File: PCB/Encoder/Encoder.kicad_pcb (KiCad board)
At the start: 2 copper layers, 44.3 x 44.8 mm, 8 parts, among them J1 1-1734595-0 Header, U1 AS5047P-ATSM

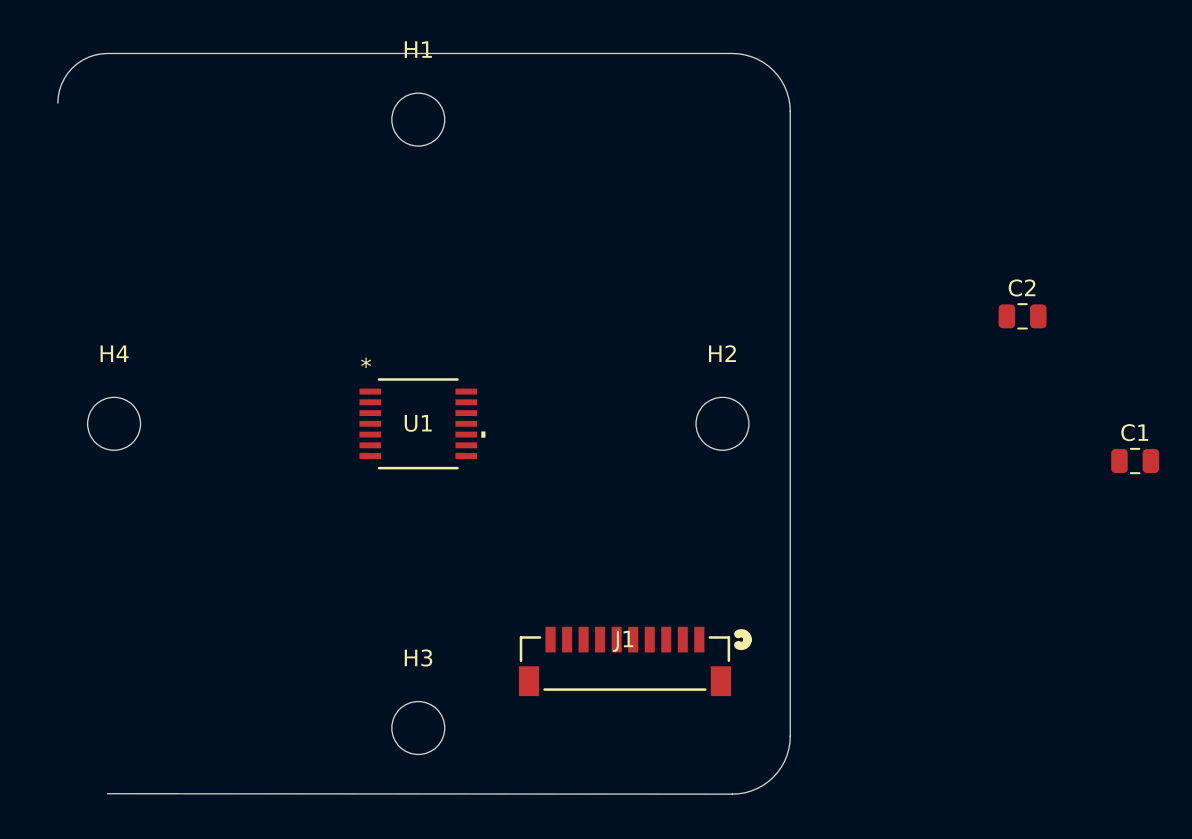
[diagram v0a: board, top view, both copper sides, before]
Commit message: Fixed GroundDetch not grounded
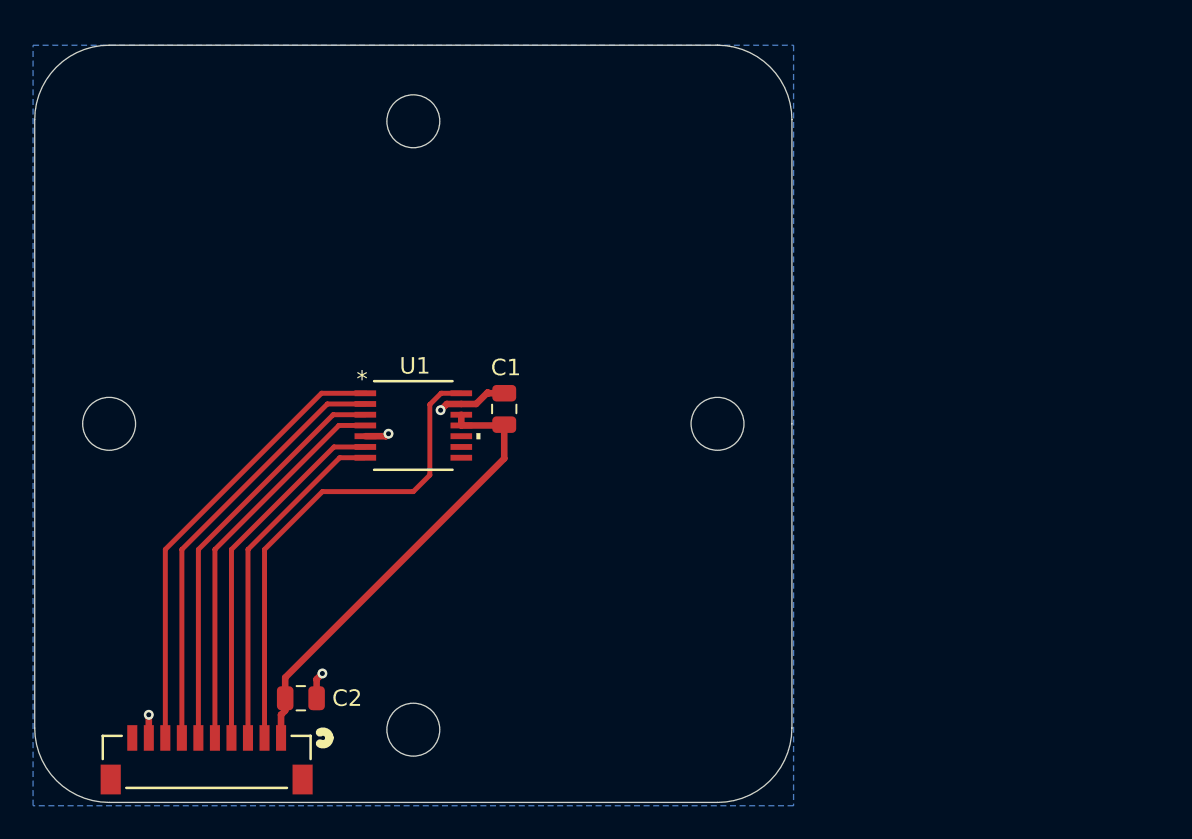
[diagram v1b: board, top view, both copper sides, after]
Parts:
- moved C2 49.4 mm to (125.2, 99.0)
- moved C1 38.3 mm to (137.5, 81.5), turned to 90 degrees
- moved J1 26.0 mm to (119.5, 102.8)
- moved H3 0.32 mm to (132.0, 100.9)
- moved H1 0.32 mm to (132.0, 64.1)
- moved U1 0.32 mm to (132.0, 82.5)
- moved H4 0.30 mm to (113.6, 82.4)
- moved H2 0.30 mm to (150.4, 82.4)
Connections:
- J1 pad 2: CS_ -> I
- J1 pad 3: CLK -> B
- J1 pad 4: MISO -> A
- J1 pad 6: A -> MISO
- J1 pad 7: B -> CLK
- J1 pad 8: I -> CS_
- U1 pad 5: Net-(U1-TEST) -> GND
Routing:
- net I: track 0.00 -> 29.7 mm
- net +3.3V: track 0.00 -> 27.9 mm
- net CS_: track 0.00 -> 27.4 mm
- net CLK: track 0.00 -> 26.1 mm
- net MISO: track 0.00 -> 24.9 mm
- net MOSI: track 0.00 -> 23.6 mm
- net A: track 0.00 -> 22.1 mm
- net B: track 0.00 -> 20.8 mm
- net GND: track 0.00 -> 8.83 mm, vias 0 -> 4
- added copper zone on B.Cu, net GND
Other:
- board size 44.3 x 44.8 mm -> 45.8 x 45.8 mm

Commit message: Connectors wrong side fixed, PCB v1.0 Done
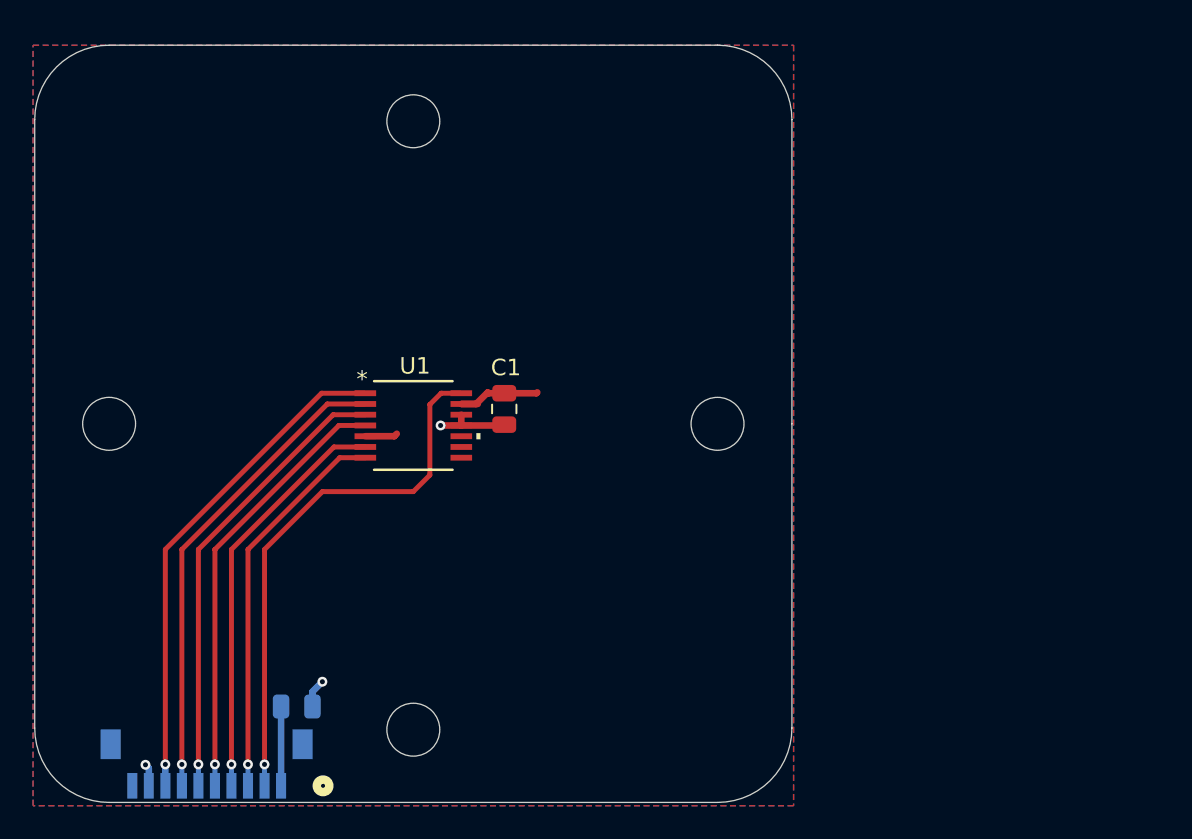
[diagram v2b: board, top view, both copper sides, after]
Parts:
- C2, J1: moved to B.Cu
- moved C2 0.56 mm to (125.0, 99.5)
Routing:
- net +3.3V: track 27.9 -> 9.39 mm, vias 0 -> 1
- net MOSI: track 23.6 -> 26.5 mm, vias 0 -> 1
- net MISO: track 24.9 -> 27.8 mm, vias 0 -> 1
- net I: track 29.7 -> 32.6 mm, vias 0 -> 1
- net CS_: track 27.4 -> 30.3 mm, vias 0 -> 1
- net CLK: track 26.1 -> 29.0 mm, vias 0 -> 1
- net B: track 20.8 -> 23.7 mm, vias 0 -> 1
- net A: track 22.1 -> 25.0 mm, vias 0 -> 1
- net GND: track 8.83 -> 11.0 mm, vias 4 -> 2
- added copper zone on B.Cu, net +3.3V
- added copper zone on F.Cu, net GND
- removed copper zone on B.Cu, net GND
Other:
- board text added: "v1.0 7/17/24"
- board text added: "•X •GND •CS_ •CLK •MISO •MOSI •A •B •I •3.3V"
